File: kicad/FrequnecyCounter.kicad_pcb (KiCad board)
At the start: 4 copper layers, 130 x 90 mm, 144 parts, among them J1 USB_B, J2 CONN_COAXIAL, J3 CONN_COAXIAL, J4 CONN_COAXIAL, Q1 BC846B, T1 WBC16-1T, U1 TPS650250, U10 MC12093, U11 tx176, U12 TLV3501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

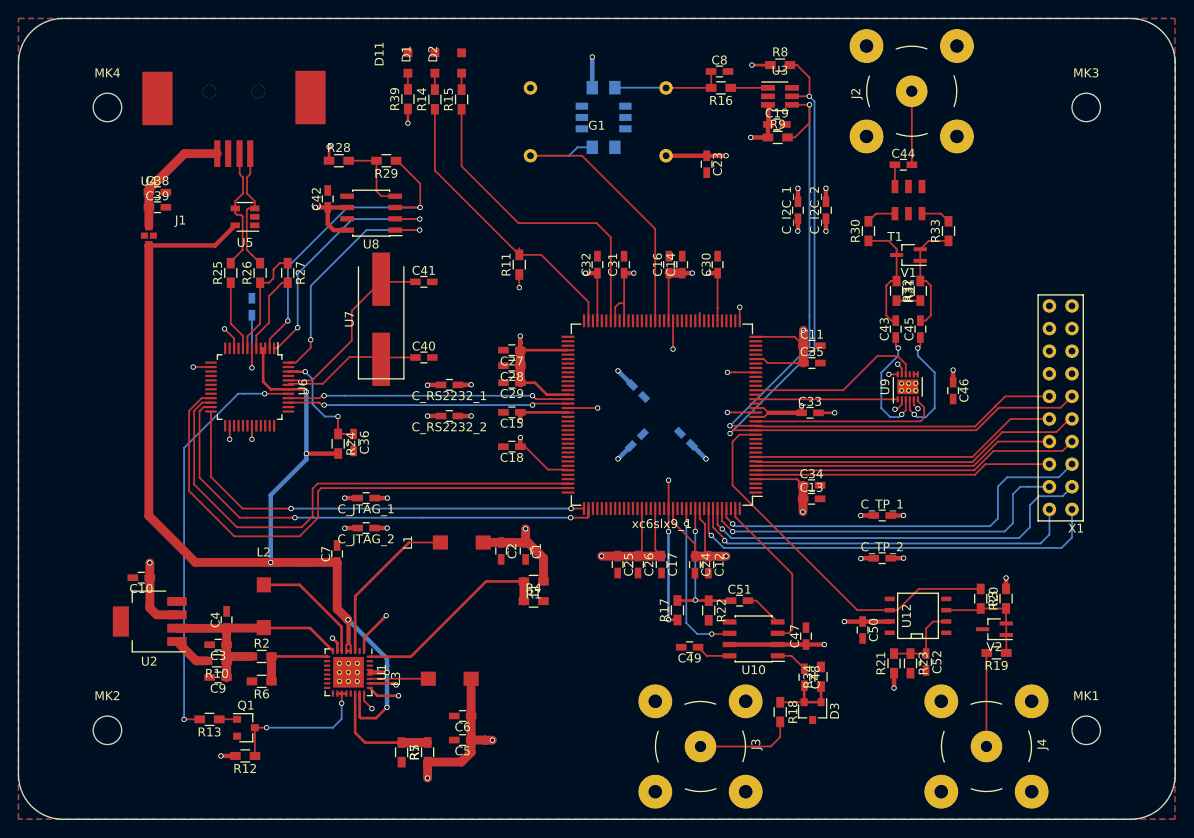
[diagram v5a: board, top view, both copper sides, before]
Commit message: Relocated overhanging USB connector
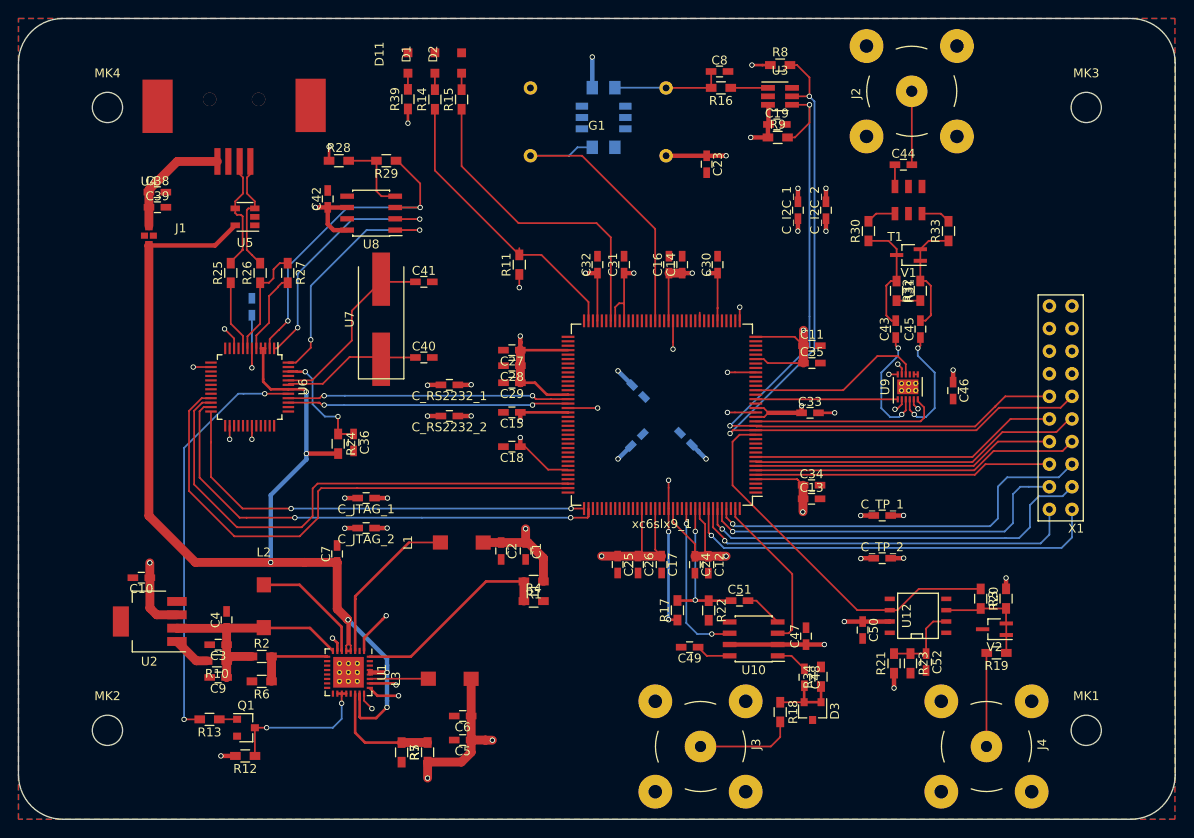
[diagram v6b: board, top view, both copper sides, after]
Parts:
- moved J1 0.88 mm to (88.2, 79.1)
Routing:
- net /USB_JTAG/D-: track 13.9 -> 13.1 mm
- net /USB_JTAG/D+: track 14.2 -> 13.4 mm
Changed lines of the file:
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@@
     (2 In2.Cu power)
     (31 B.Cu signal)
-    (32 B.Adhes user)
-    (33 F.Adhes user)
-    (34 B.Paste user)
-    (35 F.Paste user)
+    (32 B.Adhes user hide)
+    (33 F.Adhes user hide)
+    (34 B.Paste user hide)
+    (35 F.Paste user hide)
     (36 B.SilkS user)
     (37 F.SilkS user)
     (38 B.Mask user)
     (39 F.Mask user)
-    (40 Dwgs.User user)
+    (40 Dwgs.User user hide)
     (41 Cmts.User user)
-    (42 Eco1.User user)
-    (43 Eco2.User user)
+    (42 Eco1.User user hide)
+    (43 Eco2.User user hide)
     (44 Edge.Cuts user)
-    (45 Margin user)
+    (45 Margin user hide)
     (46 B.CrtYd user)
     (47 F.CrtYd user)
@@
     (mod_text_size 1 1)
     (mod_text_width 0.15)
-    (pad_size 3 0.7)
-    (pad_drill 0)
+    (pad_size 3.4 3.4)
+    (pad_drill 3.4)
     (pad_to_mask_clearance 0.2)
     (aux_axis_origin 69.97 146)
@@
   )
   (module Footprints_LJ:USB_B_liegen_SMD (layer F.Cu)
-    (at 88.22 78.19)
+    (at 88.235 79.07)
     (fp_text reference J1 (at 0 0.5) (layer F.SilkS)
       (effects (font (size 1 1) (thickness 0.15)))
@@
     (fp_circle (center 0 0) (end 2.85 0) (layer Cmts.User) (width 0.15))
     (fp_circle (center 0 0) (end 3.1 0) (layer F.CrtYd) (width 0.05))
-    (pad 1 np_thru_hole circle (at 0 0) (size 3.2 3.2) (drill 3.2) (layers *.Cu *.Mask))
+    (pad "" np_thru_hole circle (at 0 0) (size 3.4 3.4) (drill 3.4) (layers *.Cu *.Mask))
   )
   (module Mounting_Holes:MountingHole_3.2mm_M3_ISO7380 (layer F.Cu)
@@
     (fp_circle (center 0 0) (end 2.85 0) (layer Cmts.User) (width 0.15))
     (fp_circle (center 0 0) (end 3.1 0) (layer F.CrtYd) (width 0.05))
-    (pad 1 np_thru_hole circle (at 0 0) (size 3.2 3.2) (drill 3.2) (layers *.Cu *.Mask))
+    (pad "" np_thru_hole circle (at 0 0) (size 3.4 3.4) (drill 3.4) (layers *.Cu *.Mask))
   )
   (module Mounting_Holes:MountingHole_3.2mm_M3_ISO7380 (layer F.Cu)
@@
     (fp_circle (center 0 0) (end 2.85 0) (layer Cmts.User) (width 0.15))
     (fp_circle (center 0 0) (end 3.1 0) (layer F.CrtYd) (width 0.05))
-    (pad 1 np_thru_hole circle (at 0 0) (size 3.2 3.2) (drill 3.2) (layers *.Cu *.Mask))
+    (pad "" np_thru_hole circle (at 0 0) (size 3.4 3.4) (drill 3.4) (layers *.Cu *.Mask))
   )
   (module Mounting_Holes:MountingHole_3.2mm_M3_ISO7380 (layer F.Cu)
@@
     (fp_circle (center 0 0) (end 2.85 0) (layer Cmts.User) (width 0.15))
     (fp_circle (center 0 0) (end 3.1 0) (layer F.CrtYd) (width 0.05))
-    (pad 1 np_thru_hole circle (at 0 0) (size 3.2 3.2) (drill 3.2) (layers *.Cu *.Mask))
+    (pad "" np_thru_hole circle (at 0 0) (size 3.4 3.4) (drill 3.4) (layers *.Cu *.Mask))
   )
   (module Footprints_LJ:Mini_TopLed_SMD (layer F.Cu)
@@
   (gr_arc (start 75 141) (end 75 146) (angle 90) (layer Edge.Cuts) (width 0.15))
   (gr_arc (start 75 61) (end 70 61) (angle 90) (layer Edge.Cuts) (width 0.15))
-  (gr_text +3.3V (at 93.58 114.11) (layer F.CrtYd)
+  (gr_text +3.3V (at 78.06 114.38) (layer F.CrtYd)
     (effects (font (size 1.5 1.5) (thickness 0.3)))
   )
@@
   (segment (start 96.2339 94.80686) (end 96.2339 95.2661) (width 0.2) (layer F.Cu) (net 6))
   (segment (start 96.2339 94.80686) (end 96.2339 93.0742) (width 0.2) (layer F.Cu) (net 6))
-  (segment (start 84.66 75.184998) (end 88.654998 71.19) (width 1) (layer F.Cu) (net 7))
-  (segment (start 84.66 75.52) (end 84.66 75.184998) (width 1) (layer F.Cu) (net 7))
-  (segment (start 88.654998 71.19) (end 92.345 71.19) (width 1) (layer F.Cu) (net 7))
+  (segment (start 84.66 75.52) (end 84.66 75.256998) (width 1) (layer F.Cu) (net 7))
+  (segment (start 84.66 75.256998) (end 87.846998 72.07) (width 1) (layer F.Cu) (net 7))
+  (segment (start 92.36 72.07) (end 87.846998 72.07) (width 1) (layer F.Cu) (net 7))
   (segment (start 84.66 79.31) (end 84.66 77.2237) (width 1) (layer F.Cu) (net 7))
   (segment (start 84.66 77.2237) (end 84.6673 77.2164) (width 1) (layer F.Cu) (net 7))
@@
   (segment (start 99.26 91) (end 99.27 91) (width 0.2) (layer F.Cu) (net 93))
   (segment (start 98.2339 93.0742) (end 98.2339 92.0261) (width 0.2) (layer F.Cu) (net 93))
-  (segment (start 94.86 73.49) (end 95.233 73.863) (width 0.2) (layer F.Cu) (net 94))
-  (segment (start 94.86 71.24) (end 94.86 73.49) (width 0.2) (layer F.Cu) (net 94))
-  (segment (start 95.233 73.863) (end 95.233 75.679) (width 0.2) (layer F.Cu) (net 94))
-  (segment (start 94.36 76.552) (end 94.36 77.347) (width 0.2) (layer F.Cu) (net 94))
-  (segment (start 95.233 75.679) (end 94.36 76.552) (width 0.2) (layer F.Cu) (net 94))
+  (segment (start 94.36 77.347) (end 94.36 76.552) (width 0.2) (layer F.Cu) (net 94))
+  (segment (start 94.36 76.552) (end 95.233 75.679) (width 0.2) (layer F.Cu) (net 94))
+  (segment (start 95.233 75.679) (end 95.233 73.863) (width 0.2) (layer F.Cu) (net 94))
+  (segment (start 95.233 73.863) (end 94.86 73.49) (width 0.2) (layer F.Cu) (net 94))
+  (segment (start 94.86 73.49) (end 94.86 72.07) (width 0.2) (layer F.Cu) (net 94))
   (segment (start 95.19 82) (end 95.19 82.02) (width 0.2) (layer F.Cu) (net 94))
   (segment (start 95.19 82.02) (end 93.86 83.35) (width 0.2) (layer F.Cu) (net 94))
@@
   (segment (start 94.56 78.0664) (end 95.0264 78.0664) (width 0.2) (layer F.Cu) (net 94))
   (segment (start 95.0264 78.0664) (end 95.195601 78.235601) (width 0.2) (layer F.Cu) (net 94))
-  (segment (start 96.06 71.24) (end 96.06 73.49) (width 0.2) (layer F.Cu) (net 95))
-  (segment (start 96.06 73.49) (end 95.687 73.863) (width 0.2) (layer F.Cu) (net 95))
-  (segment (start 95.687 73.863) (end 95.687 75.679) (width 0.2) (layer F.Cu) (net 95))
-  (segment (start 95.687 75.679) (end 96.56 76.552) (width 0.2) (layer F.Cu) (net 95))
-  (segment (start 96.56 76.552) (end 96.56 77.347) (width 0.2) (layer F.Cu) (net 95))
+  (segment (start 96.56 77.347) (end 96.56 76.552) (width 0.2) (layer F.Cu) (net 95))
+  (segment (start 96.56 76.552) (end 95.687 75.679) (width 0.2) (layer F.Cu) (net 95))
+  (segment (start 96.06 73.49) (end 96.06 72.07) (width 0.2) (layer F.Cu) (net 95))
+  (segment (start 95.687 75.679) (end 95.687 73.863) (width 0.2) (layer F.Cu) (net 95))
+  (segment (start 95.687 73.863) (end 96.06 73.49) (width 0.2) (layer F.Cu) (net 95))
   (segment (start 96.26 82.6) (end 97.16 83.5) (width 0.2) (layer F.Cu) (net 95))
   (segment (start 95.66 82) (end 96.26 82.6) (width 0.2) (layer F.Cu) (net 95))

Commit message: Placed vias to stitch gnd planes together | Add blank pcb frame | Changed some panel positions
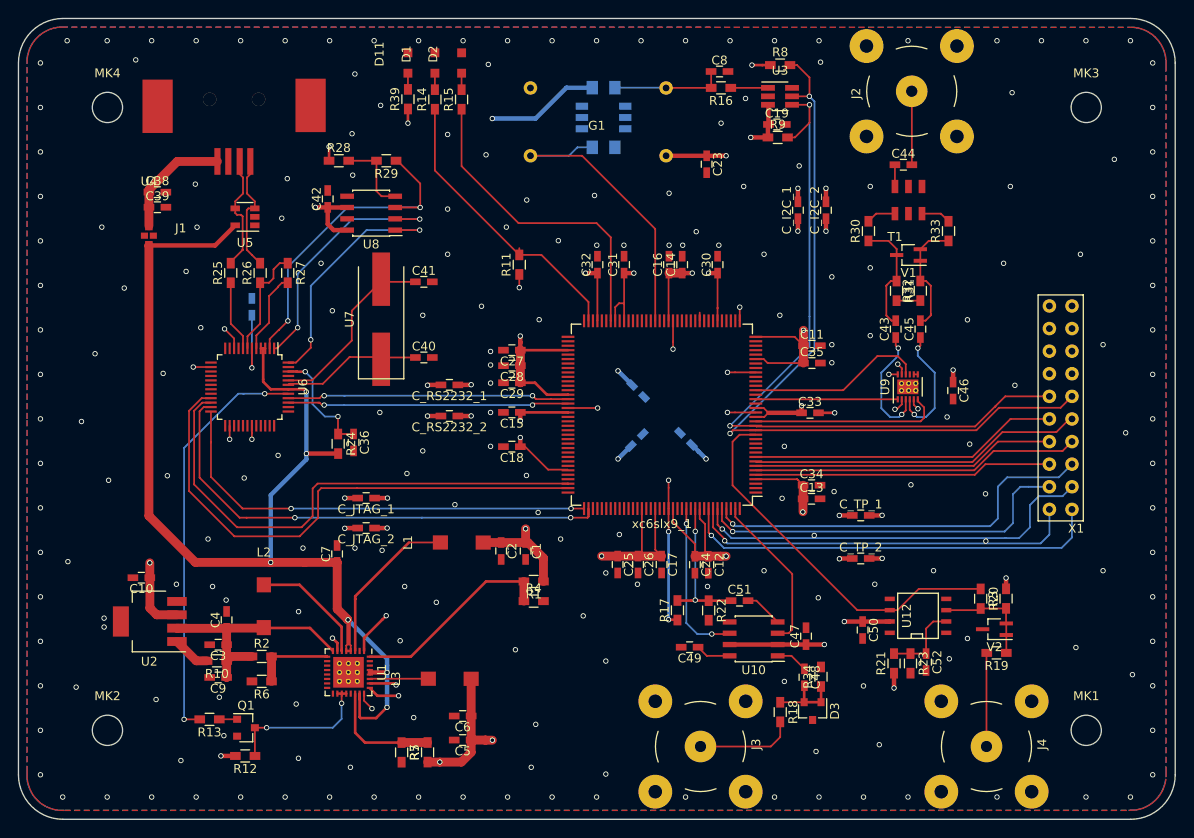
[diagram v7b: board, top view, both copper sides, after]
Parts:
- moved C_TP_2 2.41 mm to (164.7, 116.7)
- moved C_TP_1 2.41 mm to (164.7, 111.8)
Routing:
- net (no net): track 778.9 -> 754.5 mm, vias 0 -> 208
- net +3V3: track 81.6 -> 90.9 mm
- net +3V3_FPGA: track 159.6 -> 157.8 mm
- added copper zone on In2.Cu, net GND

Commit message: layout commit after generating Gerberfiles
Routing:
- net (no net): vias 208 -> 205
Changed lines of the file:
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@@
     (links 380)
     (no_connects 0)
-    (area 69.924999 55.924999 200.075001 146.075001)
+    (area 39.150001 34.03 200.075001 155.795001)
     (thickness 1.6)
-    (drawings 44)
-    (tracks 1147)
+    (drawings 32)
+    (tracks 1144)
     (zones 0)
     (modules 144)
@@
     (2 In2.Cu power)
     (31 B.Cu signal)
-    (32 B.Adhes user)
-    (33 F.Adhes user)
+    (32 B.Adhes user hide)
+    (33 F.Adhes user hide)
     (34 B.Paste user)
     (35 F.Paste user)
-    (36 B.SilkS user)
-    (37 F.SilkS user)
+    (36 B.SilkS user hide)
+    (37 F.SilkS user hide)
     (38 B.Mask user)
     (39 F.Mask user)
-    (40 Dwgs.User user)
-    (41 Cmts.User user)
-    (42 Eco1.User user)
-    (43 Eco2.User user)
+    (40 Dwgs.User user hide)
+    (41 Cmts.User user hide)
+    (42 Eco1.User user hide)
+    (43 Eco2.User user hide)
     (44 Edge.Cuts user)
-    (45 Margin user)
+    (45 Margin user hide)
     (46 B.CrtYd user)
     (47 F.CrtYd user)
@@
     (visible_elements 7FFFFFFF)
     (pcbplotparams
-      (layerselection 0x38030_80000007)
+      (layerselection 0x3d0cc_80000007)
       (usegerberextensions false)
       (excludeedgelayer true)
@@
       (padsonsilk false)
       (subtractmaskfromsilk false)
-      (outputformat 4)
+      (outputformat 1)
       (mirror false)
       (drillshape 0)
@@
     )
   )
+  (gr_line (start 72.08 60.8) (end 72.09 141.3) (layer B.Mask) (width 4))
   (gr_arc (start 194.944001 61.017668) (end 195.269782 58.056596) (angle 86.2) (layer B.Mask) (width 4))
   (gr_line (start 197.95 141.24) (end 197.94 61.08) (layer B.Mask) (width 4))
@@
   (gr_arc (start 75.045999 140.962332) (end 74.720218 143.923404) (angle 86.2) (layer B.Mask) (width 4))
   (gr_arc (start 75.047668 61.045999) (end 72.086596 60.720218) (angle 86.2) (layer B.Mask) (width 4))
-  (gr_line (start 72.08 60.8) (end 72.09 141.3) (layer B.Mask) (width 4))
   (gr_line (start 195.15 58.08) (end 74.88 58.07) (layer B.Mask) (width 4))
   (gr_arc (start 194.944001 61.017668) (end 195.269782 58.056596) (angle 86.26756471) (layer F.Mask) (width 4))
   (gr_arc (start 194.952332 140.954001) (end 197.913404 141.279782) (angle 86.26756471) (layer F.Mask) (width 4))
   (gr_arc (start 75.045999 140.962332) (end 74.720218 143.923404) (angle 86.26756471) (layer F.Mask) (width 4))
-  (gr_arc (start 194.937509 61.041072) (end 195.12329 57.55) (angle 89.5) (layer B.Mask) (width 3))
-  (gr_line (start 198.43 141.27) (end 198.43 61.2) (layer B.Mask) (width 3))
-  (gr_arc (start 194.956864 140.947509) (end 198.447936 141.13329) (angle 89.5) (layer B.Mask) (width 3))
-  (gr_line (start 195.03 144.44) (end 74.86 144.44) (layer B.Mask) (width 3))
-  (gr_arc (start 75.055781 140.958928) (end 74.87 144.45) (angle 89.5) (layer B.Mask) (width 3))
-  (gr_line (start 71.56 60.79) (end 71.57 141.29) (layer B.Mask) (width 3))
-  (gr_arc (start 75.041072 61.035781) (end 71.55 60.85) (angle 89.5) (layer B.Mask) (width 3))
-  (gr_line (start 195.1 57.56) (end 75.06 57.55) (layer B.Mask) (width 3))
   (gr_line (start 197.95 141.24) (end 197.94 61.08) (layer F.Mask) (width 4))
   (gr_line (start 195.1 143.94) (end 74.77 143.93) (layer F.Mask) (width 4))
@@
   (gr_arc (start 75.047668 61.045999) (end 72.086596 60.720218) (angle 86.26756471) (layer F.Mask) (width 4))
   (gr_line (start 195.15 58.08) (end 74.88 58.07) (layer F.Mask) (width 4))
-  (gr_arc (start 195.018319 60.955001) (end 194.92 56.49) (angle 95.22405738) (layer Margin) (width 1))
-  (gr_arc (start 195.014999 141.028319) (end 199.48 140.93) (angle 95.22405738) (layer Margin) (width 1))
-  (gr_arc (start 74.935407 141.048631) (end 75.033726 145.513632) (angle 95.22405738) (layer Margin) (width 1))
-  (gr_arc (start 74.935001 60.931681) (end 70.47 61.03) (angle 95.22405738) (layer Margin) (width 1))
   (gr_line (start 200 141) (end 200 141) (layer Edge.Cuts) (width 0.15))
   (gr_line (start 200 61) (end 200 141) (layer Edge.Cuts) (width 0.15))
@@
   (via (at 157.74 72.57) (size 0.6) (drill 0.4) (layers F.Cu B.Cu) (net 0))
   (via (at 181.67 64.34) (size 0.6) (drill 0.4) (layers F.Cu B.Cu) (net 0))
-  (via (at 178.72 114.74) (size 0.6) (drill 0.4) (layers F.Cu B.Cu) (net 0))
-  (via (at 159.43 114.1) (size 0.6) (drill 0.4) (layers F.Cu B.Cu) (net 0))
   (via (at 128.52 89.85) (size 0.6) (drill 0.4) (layers F.Cu B.Cu) (net 0))
   (via (at 81.89 86.3) (size 0.6) (drill 0.4) (layers F.Cu B.Cu) (net 0))
   (via (at 76.48 131.15) (size 0.6) (drill 0.4) (layers F.Cu B.Cu) (net 0))
   (via (at 127.09 107.36) (size 0.6) (drill 0.4) (layers F.Cu B.Cu) (net 0))
-  (via (at 128.4 111.52) (size 0.6) (drill 0.4) (layers F.Cu B.Cu) (net 0))
-  (via (at 119.05 110.64) (size 0.6) (drill 0.4) (layers F.Cu B.Cu) (net 0))
+  (via (at 119.97 110) (size 0.6) (drill 0.4) (layers F.Cu B.Cu) (net 0))
   (segment (start 162.17 60.22) (end 162.12 60.17) (width 0.2) (layer In2.Cu) (net 0))
   (segment (start 162.12 60.17) (end 74.97 60.17) (width 0.2) (layer In2.Cu) (net 0))
